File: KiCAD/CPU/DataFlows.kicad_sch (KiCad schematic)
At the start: 24 parts

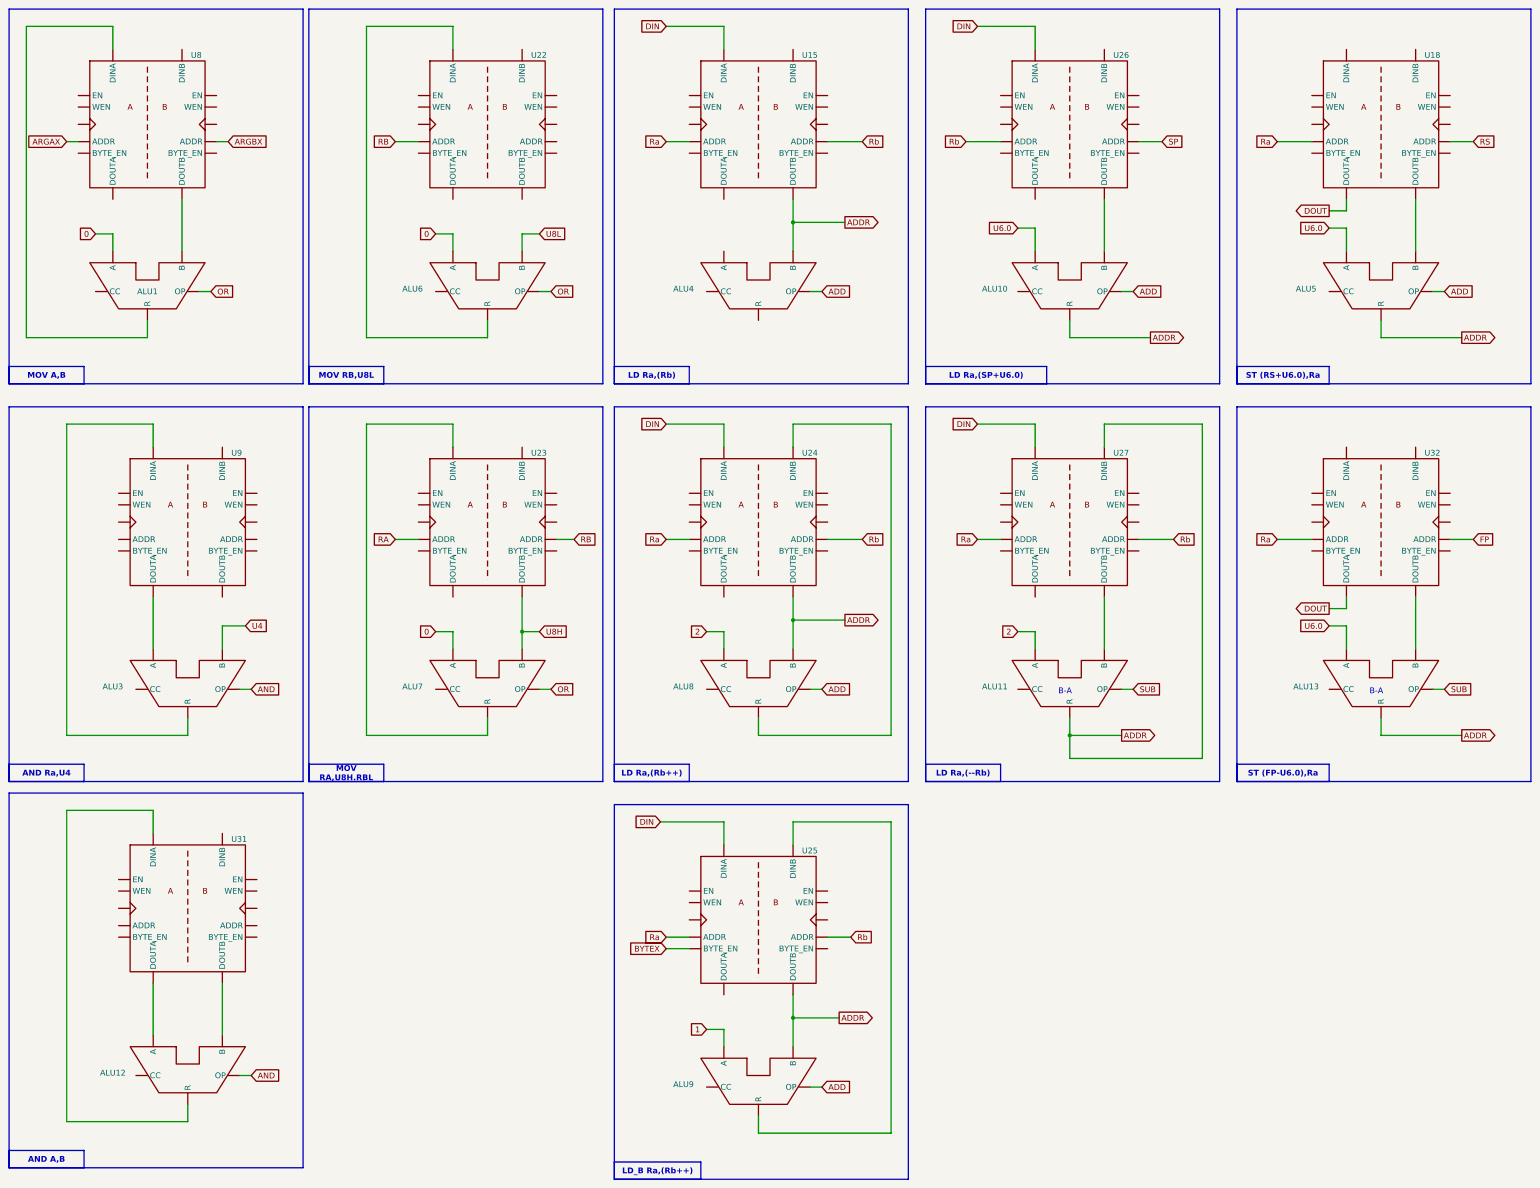
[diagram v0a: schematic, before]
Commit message: Started design of debugV2 with snooping
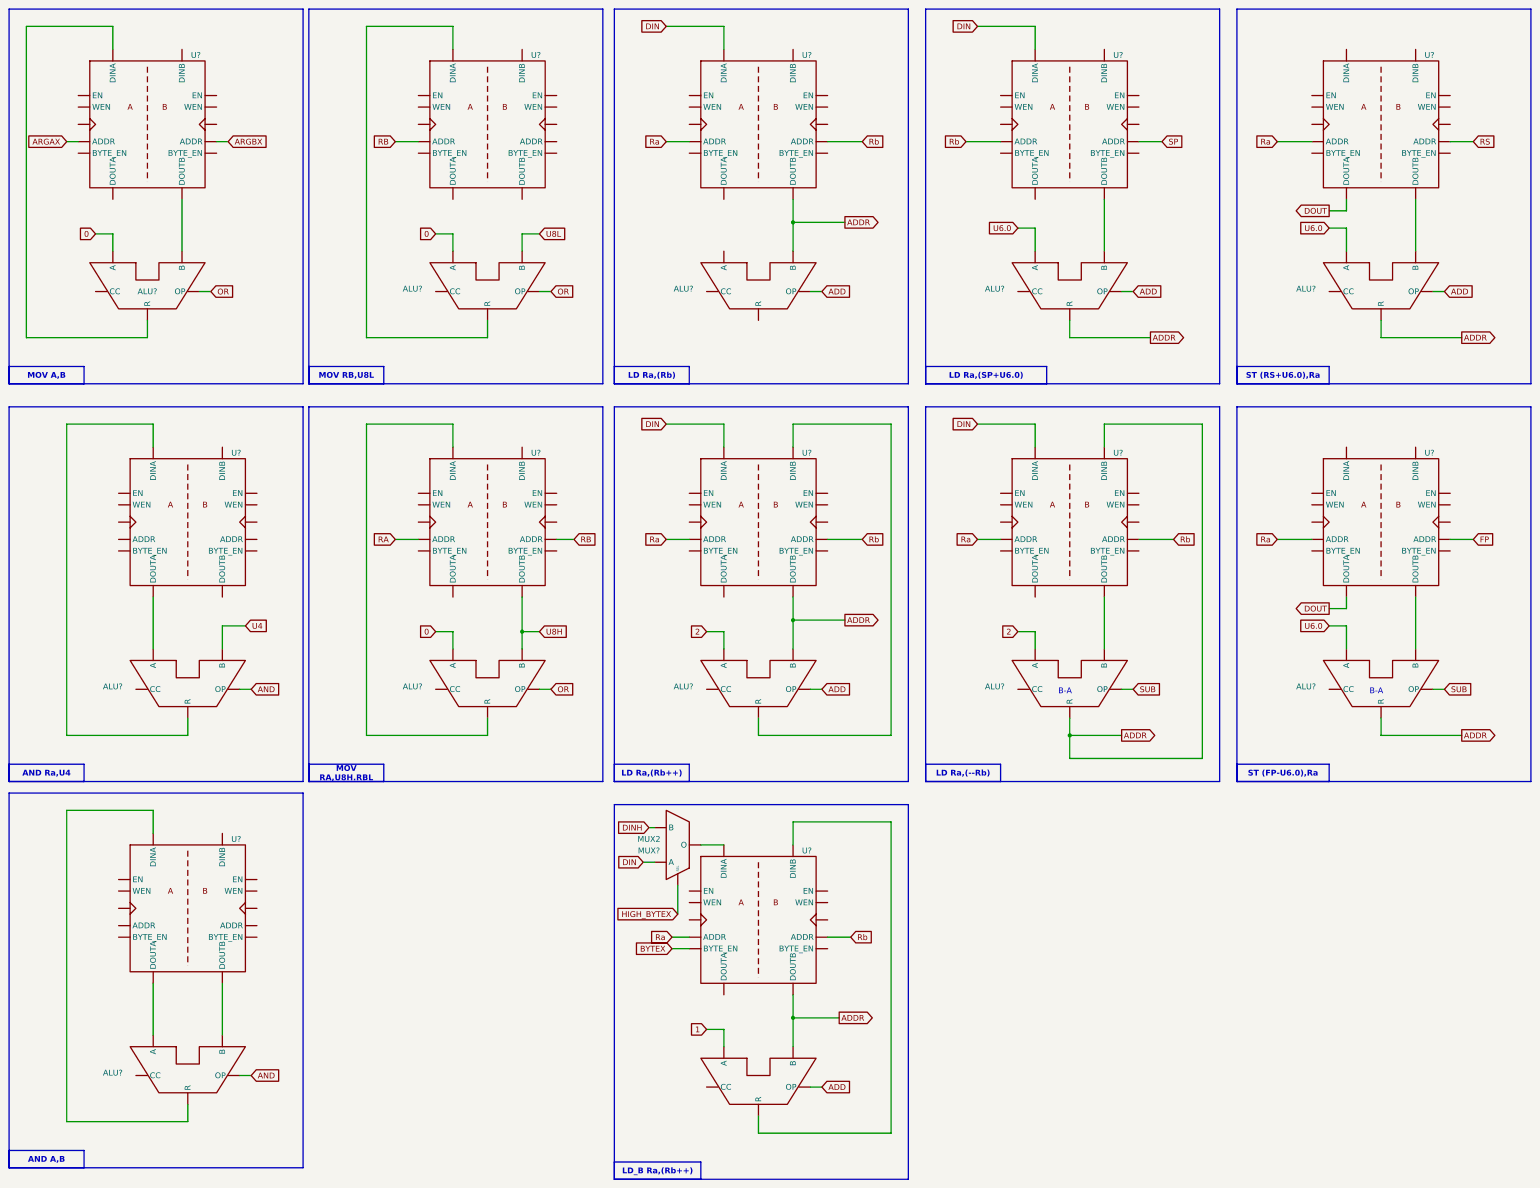
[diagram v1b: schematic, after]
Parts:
- added MUX?: MUX2, symbol UKMaker:Generic_MUX2
- renumbered ALU9 to ALU?, ALU3 to ALU?, ALU12 to ALU?, ALU10 to ALU?, ALU5 to ALU?, ALU4 to ALU?, ALU13 to ALU?, ALU6 to ALU?, ALU11 to ALU?, ALU7 to ALU?, ALU1 to ALU?, ALU8 to ALU?, U27 to U?, U26 to U?, U31 to U?, U18 to U?, U22 to U?, U15 to U?, U8 to U?, U25 to U?, U9 to U?, U23 to U?, U24 to U?, U32 to U?
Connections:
- net DIN: now also MUX?. (SEL); no longer U?. (WEN)
- net at U?. (WEN): no longer ALU?. (R)
- net at U?. (WEN): now also ALU?. (R)
- new net: ALU?. (R), U?. (WEN) (x14)
- new net: MUX?. (SEL), U?. (WEN)
- new net DINH: MUX?. (SEL)
- new net HIGH_BYTEX: MUX?. (SEL)
- now unconnected: U?. (WEN)
